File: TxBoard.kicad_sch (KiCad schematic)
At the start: 14 parts, among them J1 RCA Socket, Q1 RU1J002YNTCL, SW1 Pull-Up, SW2 Input/Output, SW3 Low/High, SW4 Low/Hi-Z

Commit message: Name Change
Me, indecisive? Never.
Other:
- title: TxBoard Communications Education Board -> TixBoard Communications Education Board
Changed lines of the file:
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@@
   (paper "A4")
   (title_block
-    (title "TxBoard Communications Education Board")
+    (title "TixBoard Communications Education Board")
     (date "2022-04-14")
     (rev "1")

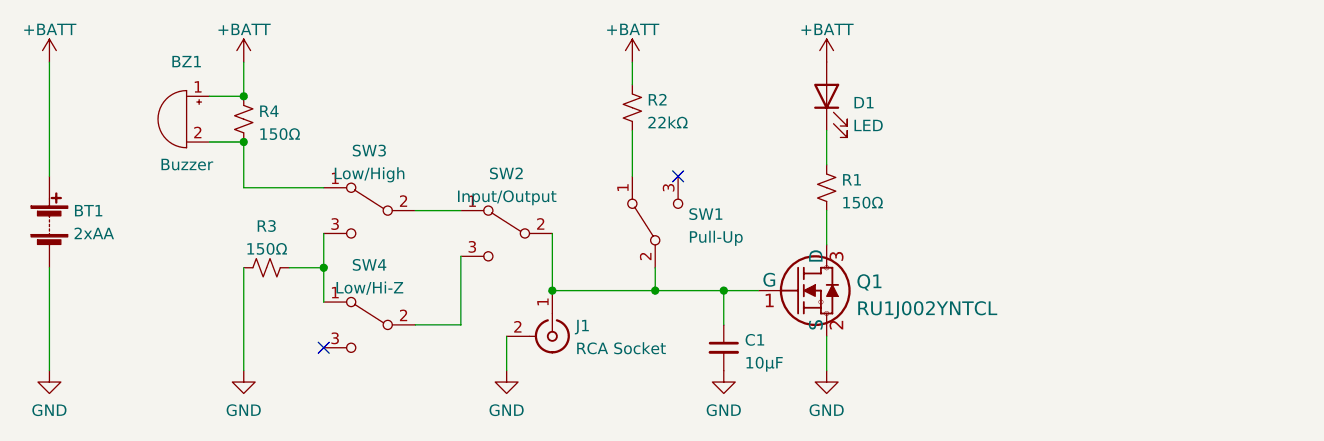
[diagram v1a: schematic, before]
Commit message: Schematic (mostly) finished
Removed libraries because I really rather not open that can of legal worms. Gonna have to find them yourself.
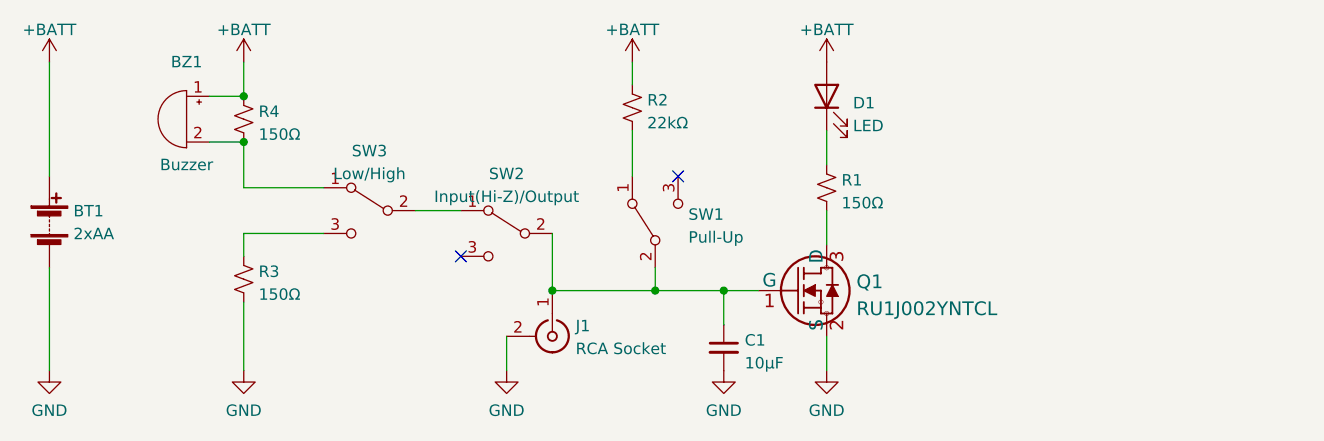
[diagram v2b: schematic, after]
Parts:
- removed SW4: Low/Hi-Z, symbol Switch:SW_SPDT
- BT1: footprint (none) -> BC2AAPC:BAT_BC2AAPC
- BZ1: footprint (none) -> PKM13EPYH4000-A0:SPKR_PKM13EPYH4000-A0
- SW1, SW3: footprint (none) -> EG1218:EG1218
- SW2: value Input/Output -> Input(Hi-Z)/Output; footprint (none) -> EG1218:EG1218
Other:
- moved on the sheet: R3
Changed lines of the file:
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@@
     (rev "1")
     (company "QuarterWave Engineering")
-    (comment 1 "MOSFET changed to more suitable model with lower Vth")
-    (comment 2 "Design Changes: Hi-Z/Low switch added to input, cost reduction,")
+    (comment 2 "Design Changes: Cost reduction, MOSFET changed to more suitable model with lower Vth")
     (comment 3 "Original Idea and design: https://twitter.com/m_ou_se/status/1511085846769848329")
     (comment 4 "[Designed with <3 in San Diego - Licensed under MIT License]")
@@
   (junction (at 154.94 104.14) (diameter 0) (color 0 0 0 0)
   )
-  (junction (at 129.54 101.6) (diameter 0) (color 0 0 0 0)
-  )
   (junction (at 120.65 82.55) (diameter 0) (color 0 0 0 0)
   )
@@
   (junction (at 166.37 104.14) (diameter 0) (color 0 0 0 0)
   )
-  (no_connect (at 129.54 110.49))
+  (no_connect (at 144.78 100.33))
   (no_connect (at 168.91 91.44))
   (wire (pts (xy 185.42 86.36) (xy 185.42 90.17))
@@
     (stroke (width 0) (type default) (color 0 0 0 0))
   )
-  (wire (pts (xy 125.73 101.6) (xy 129.54 101.6))
-    (stroke (width 0) (type default) (color 0 0 0 0))
-  )
   (wire (pts (xy 166.37 104.14) (xy 154.94 104.14))
     (stroke (width 0) (type default) (color 0 0 0 0))
@@
     (stroke (width 0) (type default) (color 0 0 0 0))
   )
-  (wire (pts (xy 144.78 100.33) (xy 144.78 107.95))
-    (stroke (width 0) (type default) (color 0 0 0 0))
-  )
   (wire (pts (xy 173.99 104.14) (xy 177.8 104.14))
     (stroke (width 0) (type default) (color 0 0 0 0))
   )
-  (wire (pts (xy 120.65 101.6) (xy 120.65 113.03))
+  (wire (pts (xy 129.54 97.79) (xy 120.65 97.79))
     (stroke (width 0) (type default) (color 0 0 0 0))
   )
@@
     (stroke (width 0) (type default) (color 0 0 0 0))
   )
-  (wire (pts (xy 129.54 101.6) (xy 129.54 105.41))
-    (stroke (width 0) (type default) (color 0 0 0 0))
-  )
   (wire (pts (xy 166.37 104.14) (xy 166.37 101.6))
     (stroke (width 0) (type default) (color 0 0 0 0))
   )
-  (wire (pts (xy 144.78 107.95) (xy 139.7 107.95))
-    (stroke (width 0) (type default) (color 0 0 0 0))
-  )
-  (wire (pts (xy 129.54 97.79) (xy 129.54 101.6))
+  (wire (pts (xy 120.65 105.41) (xy 120.65 113.03))
     (stroke (width 0) (type default) (color 0 0 0 0))
   )
   (wire (pts (xy 154.94 97.79) (xy 154.94 104.14))
+    (stroke (width 0) (type default) (color 0 0 0 0))
+  )
+  (wire (pts (xy 120.65 97.79) (xy 120.65 100.33))
     (stroke (width 0) (type default) (color 0 0 0 0))
   )
@@
     (pin "2")
   )
-  (symbol (lib_id "Device:R_Small_US") (at 123.19 101.6 90) (unit 1)
-    (in_bom yes) (on_board yes) (fields_autoplaced)
-    (property "Reference" "R3" (id 0) (at 123.19 97.0112 90))
-    (property "Value" "150Ω" (id 1) (at 123.19 99.5481 90))
-    (property "Footprint" "Resistor_SMD:R_0603_1608Metric_Pad0.98x0.95mm_HandSolder" (id 2) (at 123.19 101.6 0)
-      (effects (font (size 1.27 1.27)) hide)
-    )
-    (property "Datasheet" "~" (id 3) (at 123.19 101.6 0)
-      (effects (font (size 1.27 1.27)) hide)
-    )
-    (pin "1")
-    (pin "2")
-  )
-  (symbol (lib_id "Switch:SW_SPDT") (at 134.62 107.95 0) (mirror y) (unit 1)
-    (in_bom yes) (on_board yes) (fields_autoplaced)
-    (property "Reference" "SW4" (id 0) (at 134.62 101.3292 0))
-    (property "Value" "Low/Hi-Z" (id 1) (at 134.62 103.8661 0))
-    (property "Footprint" "" (id 2) (at 134.62 107.95 0)
-      (effects (font (size 1.27 1.27)) hide)
-    )
-    (property "Datasheet" "~" (id 3) (at 134.62 107.95 0)
-      (effects (font (size 1.27 1.27)) hide)
-    )
-    (pin "1")
-    (pin "2")
-    (pin "3")
+  (symbol (lib_id "Device:R_Small_US") (at 120.65 102.87 180) (unit 1)
+    (in_bom yes) (on_board yes) (fields_autoplaced)
+    (property "Reference" "R3" (id 0) (at 122.301 102.0353 0)
+      (effects (font (size 1.27 1.27)) (justify right))
+    )
+    (property "Value" "150Ω" (id 1) (at 122.301 104.5722 0)
+      (effects (font (size 1.27 1.27)) (justify right))
+    )
+    (property "Footprint" "Resistor_SMD:R_0603_1608Metric_Pad0.98x0.95mm_HandSolder" (id 2) (at 120.65 102.87 0)
+      (effects (font (size 1.27 1.27)) hide)
+    )
+    (property "Datasheet" "~" (id 3) (at 120.65 102.87 0)
+      (effects (font (size 1.27 1.27)) hide)
+    )
+    (pin "1")
+    (pin "2")
   )
   (symbol (lib_id "power:GND") (at 149.86 113.03 0) (unit 1)
@@
       (effects (font (size 1.27 1.27)) (justify left))
     )
-    (property "Footprint" "" (id 2) (at 99.06 94.996 90)
+    (property "Footprint" "BC2AAPC:BAT_BC2AAPC" (id 2) (at 99.06 94.996 90)
       (effects (font (size 1.27 1.27)) hide)
     )
@@
     (property "Reference" "SW3" (id 0) (at 134.62 88.6292 0))
     (property "Value" "Low/High" (id 1) (at 134.62 91.1661 0))
-    (property "Footprint" "" (id 2) (at 134.62 95.25 0)
+    (property "Footprint" "EG1218:EG1218" (id 2) (at 134.62 95.25 0)
       (effects (font (size 1.27 1.27)) hide)
     )
@@
       (effects (font (size 1.27 1.27)) (justify right))
     )
-    (property "Footprint" "" (id 2) (at 166.37 96.52 0)
+    (property "Footprint" "EG1218:EG1218" (id 2) (at 166.37 96.52 0)
       (effects (font (size 1.27 1.27)) hide)
     )
@@
     (property "Reference" "BZ1" (id 0) (at 114.3 78.74 0))
     (property "Value" "Buzzer" (id 1) (at 114.3 90.17 0))
-    (property "Footprint" "" (id 2) (at 114.935 82.55 90)
+    (property "Footprint" "PKM13EPYH4000-A0:SPKR_PKM13EPYH4000-A0" (id 2) (at 114.935 82.55 90)
       (effects (font (size 1.27 1.27)) hide)
     )
@@
     (in_bom yes) (on_board yes) (fields_autoplaced)
     (property "Reference" "SW2" (id 0) (at 149.86 91.1692 0))
-    (property "Value" "Input/Output" (id 1) (at 149.86 93.7061 0))
-    (property "Footprint" "" (id 2) (at 149.86 97.79 0)
+    (property "Value" "Input(Hi-Z)/Output" (id 1) (at 149.86 93.7061 0))
+    (property "Footprint" "EG1218:EG1218" (id 2) (at 149.86 97.79 0)
       (effects (font (size 1.27 1.27)) hide)
     )
@@
     )
     (path "/4b955b5c-03e5-4624-b491-59cac36331e9"
-      (reference "BT1") (unit 1) (value "2xAA") (footprint "")
+      (reference "BT1") (unit 1) (value "2xAA") (footprint "BC2AAPC:BAT_BC2AAPC")
     )
     (path "/cee8c350-8be0-477d-80d4-b88d2f05177c"
-      (reference "BZ1") (unit 1) (value "Buzzer") (footprint "")
+      (reference "BZ1") (unit 1) (value "Buzzer") (footprint "PKM13EPYH4000-A0:SPKR_PKM13EPYH4000-A0")
     )
     (path "/6942edd1-0ba6-453d-957e-b3b7fa528bf9"
@@
     )
     (path "/c573f4f3-c4fc-4aca-ad6c-946df532b32a"
-      (reference "SW1") (unit 1) (value "Pull-Up") (footprint "")
+      (reference "SW1") (unit 1) (value "Pull-Up") (footprint "EG1218:EG1218")
     )
     (path "/d2aeeca3-2d6b-49ff-8e68-e891d2132e85"
-      (reference "SW2") (unit 1) (value "Input/Output") (footprint "")
+      (reference "SW2") (unit 1) (value "Input(Hi-Z)/Output") (footprint "EG1218:EG1218")
     )
     (path "/c3265d8f-1789-4158-aa57-27936cdaa040"
-      (reference "SW3") (unit 1) (value "Low/High") (footprint "")
-    )
-    (path "/429abe57-8581-4b4b-b32b-f76fa8c6a32e"
-      (reference "SW4") (unit 1) (value "Low/Hi-Z") (footprint "")
-    )
-  )
+      (reference "SW3") (unit 1) (value "Low/High") (footprint "EG1218:EG1218")
+    )
+  )

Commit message: Initial PCB
First crack at PCB with silkscreen and layout. Added test points
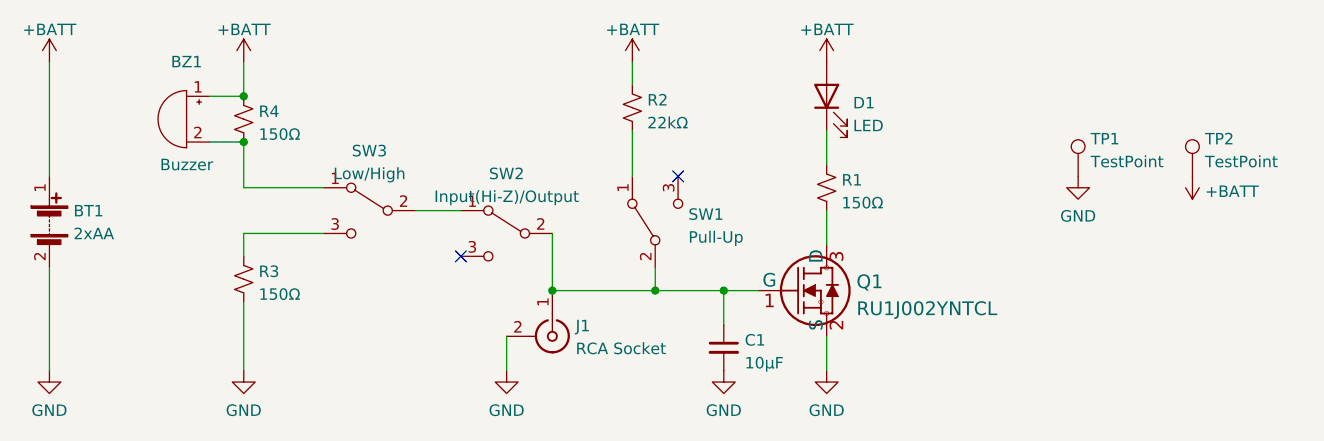
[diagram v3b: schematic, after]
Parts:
- added TP1, TP2: TestPoint, TestPoint:TestPoint_Pad_1.5x1.5mm, symbol Connector:TestPoint
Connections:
- net +BATT: now also TP2.1
- net GND: now also TP1.1
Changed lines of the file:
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@@
+    (pin "1")
+  )
+  (symbol (lib_id "power:GND") (at 213.36 91.44 0) (unit 1)
+    (in_bom yes) (on_board yes) (fields_autoplaced)
+    (property "Reference" "#PWR?" (id 0) (at 213.36 97.79 0)
+      (effects (font (size 1.27 1.27)) hide)
+    )
+    (property "Value" "GND" (id 1) (at 213.36 95.8834 0))
+    (property "Footprint" "" (id 2) (at 213.36 91.44 0)
+      (effects (font (size 1.27 1.27)) hide)
+    )
+    (property "Datasheet" "" (id 3) (at 213.36 91.44 0)
+      (effects (font (size 1.27 1.27)) hide)
+    )
     (pin "1")
   )
@@
     )
     (property "Datasheet" "" (id 3) (at 99.06 78.74 0)
+      (effects (font (size 1.27 1.27)) hide)
+    )
+    (pin "1")
+  )
+  (symbol (lib_id "power:+BATT") (at 226.06 91.44 180) (unit 1)
+    (in_bom yes) (on_board yes) (fields_autoplaced)
+    (property "Reference" "#PWR?" (id 0) (at 226.06 87.63 0)
+      (effects (font (size 1.27 1.27)) hide)
+    )
+    (property "Value" "+BATT" (id 1) (at 227.457 93.1438 0)
+      (effects (font (size 1.27 1.27)) (justify right))
+    )
+    (property "Footprint" "" (id 2) (at 226.06 91.44 0)
+      (effects (font (size 1.27 1.27)) hide)
+    )
+    (property "Datasheet" "" (id 3) (at 226.06 91.44 0)
       (effects (font (size 1.27 1.27)) hide)
     )
@@
     (pin "2")
     (pin "3")
+  )
+  (symbol (lib_id "Connector:TestPoint") (at 213.36 91.44 0) (unit 1)
+    (in_bom yes) (on_board yes) (fields_autoplaced)
+    (property "Reference" "TP1" (id 0) (at 214.757 87.3033 0)
+      (effects (font (size 1.27 1.27)) (justify left))
+    )
+    (property "Value" "TestPoint" (id 1) (at 214.757 89.8402 0)
+      (effects (font (size 1.27 1.27)) (justify left))
+    )
+    (property "Footprint" "TestPoint:TestPoint_Pad_1.5x1.5mm" (id 2) (at 218.44 91.44 0)
+      (effects (font (size 1.27 1.27)) hide)
+    )
+    (property "Datasheet" "~" (id 3) (at 218.44 91.44 0)
+      (effects (font (size 1.27 1.27)) hide)
+    )
+    (pin "1")
   )
   (symbol (lib_id "Device:Buzzer") (at 114.3 85.09 0) (mirror y) (unit 1)
@@
     (pin "3")
   )
+  (symbol (lib_id "Connector:TestPoint") (at 226.06 91.44 0) (unit 1)
+    (in_bom yes) (on_board yes) (fields_autoplaced)
+    (property "Reference" "TP2" (id 0) (at 227.457 87.3033 0)
+      (effects (font (size 1.27 1.27)) (justify left))
+    )
+    (property "Value" "TestPoint" (id 1) (at 227.457 89.8402 0)
+      (effects (font (size 1.27 1.27)) (justify left))
+    )
+    (property "Footprint" "TestPoint:TestPoint_Pad_1.5x1.5mm" (id 2) (at 231.14 91.44 0)
+      (effects (font (size 1.27 1.27)) hide)
+    )
+    (property "Datasheet" "~" (id 3) (at 231.14 91.44 0)
+      (effects (font (size 1.27 1.27)) hide)
+    )
+    (pin "1")
+  )
   (symbol (lib_id "power:GND") (at 120.65 113.03 0) (unit 1)
     (in_bom yes) (on_board yes) (fields_autoplaced)
@@
       (reference "#PWR0109") (unit 1) (value "GND") (footprint "")
     )
+    (path "/11ab8fe4-e901-4816-83cf-38a31e2afca0"
+      (reference "#PWR?") (unit 1) (value "GND") (footprint "")
+    )
+    (path "/b1231cce-7ebc-4972-bb46-0049c7c0b0dd"
+      (reference "#PWR?") (unit 1) (value "+BATT") (footprint "")
+    )
     (path "/4b955b5c-03e5-4624-b491-59cac36331e9"
       (reference "BT1") (unit 1) (value "2xAA") (footprint "BC2AAPC:BAT_BC2AAPC")
@@
       (reference "SW3") (unit 1) (value "Low/High") (footprint "EG1218:EG1218")
     )
-  )
+    (path "/cd78a05f-3030-4df8-a06c-277f5becd950"
+      (reference "TP1") (unit 1) (value "TestPoint") (footprint "TestPoint:TestPoint_Pad_1.5x1.5mm")
+    )
+    (path "/da6124c4-757b-40e4-9942-8f0ebf173eb8"
+      (reference "TP2") (unit 1) (value "TestPoint") (footprint "TestPoint:TestPoint_Pad_1.5x1.5mm")
+    )
+  )

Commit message: PCB Rev 2
Todo: TixBoard text in mask. Logo imported too thin to clear DRC
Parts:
- C1: footprint Capacitor_SMD:C_0603_1608Metric_Pad1.08x0.95mm_HandSolder -> Capacitor_SMD:C_0805_2012Metric_Pad1.18x1.45mm_HandSolder
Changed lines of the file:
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@@
       (effects (font (size 1.27 1.27)) (justify left))
     )
-    (property "Footprint" "Capacitor_SMD:C_0603_1608Metric_Pad1.08x0.95mm_HandSolder" (id 2) (at 173.99 110.49 0)
+    (property "Footprint" "Capacitor_SMD:C_0805_2012Metric_Pad1.18x1.45mm_HandSolder" (id 2) (at 173.99 110.49 0)
       (effects (font (size 1.27 1.27)) hide)
     )
@@
     )
     (path "/6942edd1-0ba6-453d-957e-b3b7fa528bf9"
-      (reference "C1") (unit 1) (value "10μF") (footprint "Capacitor_SMD:C_0603_1608Metric_Pad1.08x0.95mm_HandSolder")
+      (reference "C1") (unit 1) (value "10μF") (footprint "Capacitor_SMD:C_0805_2012Metric_Pad1.18x1.45mm_HandSolder")
     )
     (path "/1cd534f3-3a3a-4350-959a-ea3b2fc71750"

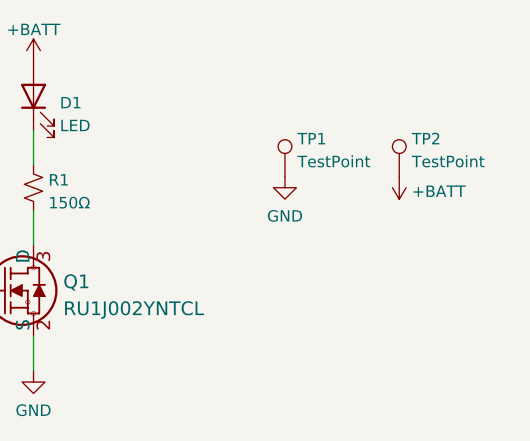
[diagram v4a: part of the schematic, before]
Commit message: Prototype 1
Board final review finished, DRC issues fixed (whoever made that RCA footprint needs to learn what the polygon tool does), production files generated and will be sent out for production soon. hope it works lol
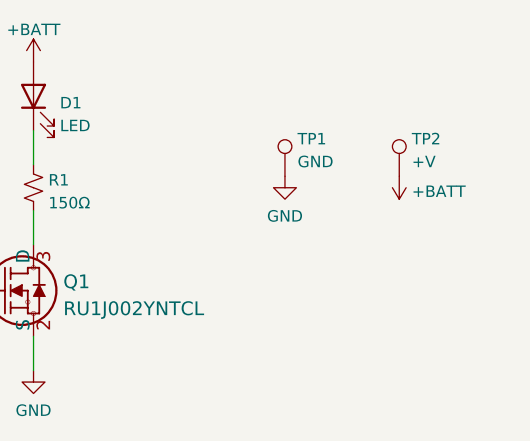
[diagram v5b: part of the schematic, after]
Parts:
- TP1: value TestPoint -> GND
- TP2: value TestPoint -> +V
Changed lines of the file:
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@@
     (title "TixBoard Communications Education Board")
     (date "2022-04-14")
-    (rev "1")
+    (rev "2")
     (company "QuarterWave Engineering")
     (comment 2 "Design Changes: Cost reduction, MOSFET changed to more suitable model with lower Vth")
@@
   (symbol (lib_id "power:GND") (at 213.36 91.44 0) (unit 1)
     (in_bom yes) (on_board yes) (fields_autoplaced)
-    (property "Reference" "#PWR?" (id 0) (at 213.36 97.79 0)
+    (property "Reference" "#PWR0110" (id 0) (at 213.36 97.79 0)
       (effects (font (size 1.27 1.27)) hide)
     )
@@
   (symbol (lib_id "power:+BATT") (at 226.06 91.44 180) (unit 1)
     (in_bom yes) (on_board yes) (fields_autoplaced)
-    (property "Reference" "#PWR?" (id 0) (at 226.06 87.63 0)
+    (property "Reference" "#PWR0111" (id 0) (at 226.06 87.63 0)
       (effects (font (size 1.27 1.27)) hide)
     )
@@
       (effects (font (size 1.27 1.27)) (justify left))
     )
-    (property "Value" "TestPoint" (id 1) (at 214.757 89.8402 0)
+    (property "Value" "GND" (id 1) (at 214.757 89.8402 0)
       (effects (font (size 1.27 1.27)) (justify left))
     )
@@
       (effects (font (size 1.27 1.27)) (justify left))
     )
-    (property "Value" "TestPoint" (id 1) (at 227.457 89.8402 0)
+    (property "Value" "+V" (id 1) (at 227.457 89.8402 0)
       (effects (font (size 1.27 1.27)) (justify left))
     )
@@
     )
     (path "/11ab8fe4-e901-4816-83cf-38a31e2afca0"
-      (reference "#PWR?") (unit 1) (value "GND") (footprint "")
+      (reference "#PWR0110") (unit 1) (value "GND") (footprint "")
     )
     (path "/b1231cce-7ebc-4972-bb46-0049c7c0b0dd"
-      (reference "#PWR?") (unit 1) (value "+BATT") (footprint "")
+      (reference "#PWR0111") (unit 1) (value "+BATT") (footprint "")
     )
     (path "/4b955b5c-03e5-4624-b491-59cac36331e9"
@@
     )
     (path "/cd78a05f-3030-4df8-a06c-277f5becd950"
-      (reference "TP1") (unit 1) (value "TestPoint") (footprint "TestPoint:TestPoint_Pad_1.5x1.5mm")
+      (reference "TP1") (unit 1) (value "GND") (footprint "TestPoint:TestPoint_Pad_1.5x1.5mm")
     )
     (path "/da6124c4-757b-40e4-9942-8f0ebf173eb8"
-      (reference "TP2") (unit 1) (value "TestPoint") (footprint "TestPoint:TestPoint_Pad_1.5x1.5mm")
-    )
-  )
+      (reference "TP2") (unit 1) (value "+V") (footprint "TestPoint:TestPoint_Pad_1.5x1.5mm")
+    )
+  )
